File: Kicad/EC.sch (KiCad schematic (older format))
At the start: 23 parts, among them U1 MCP6244

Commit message: first pass at layout
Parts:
- removed POT1, POT2, POT3, POT4, POT5, POT6, TP7: CONN_1, symbol CONN_1
- removed R10: 10K, ~, symbol R
- added C8: .1u, ~, symbol C
- added D6: DIODE, ~, symbol DIODE
- added R12: 1K, ~, symbol R
- added R2: 1.5K 1%, ~, symbol R
- added R3, R4: 22K, ~, symbol R
- added unit 1 of U1
- renumbered C9 to C5, C10 to C6, C11 to C7, D3 to D7, D5 to D8
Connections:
- net AC_Shrunk: now also R3.2
- net EC_AIN: now also R12.1, U1.1, U1.2 (-); no longer C3.1, D7.2 (K), U1.13 (-)
- net EC_ProbeIN: now also R2.2
- net EC_Signal: now also R2.1
- net VGND: now also R3.1
- net pin 14 renamed R_Vout
- net pin 5 renamed W_Vin+
- net pin 6 renamed W_Vin-
- net W_Vin-: now also R4.2
- net pin 7 renamed W_Vout
- net W_Vout: now also R4.1
- new net DD: D6.1 (A), D7.2 (K), R12.2
- new net GND: C8.2, U1.11 (V-)
- new net RVin-: C3.1, D6.2 (K), U1.13 (-), U1.3 (+)
- new net Vclean: C8.1, U1.4 (V+)
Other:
- note added: "Probe"
- note added: "Step 1: Create an AC Signal"
- note added: "Step 2: Get EC Measurement"
- note added: "Step 3: Convert AC to DC"
- note removed: "Convert AC to DC"
- note removed: "Create an AC Signal"
- note removed: "Get EC Measurement"
- moved on the sheet: C3, D7, U1D

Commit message: 2nd iteration on layout
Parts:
- removed TP1, TP12, TP20: CONN_1, symbol CONN_1
- R2: value 1.5K 1% -> 1K 1%
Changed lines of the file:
@@
 Sheet 5 8
 Title ""
-Date "17 dec 2014"
+Date "18 dec 2014"
 Rev ""
 Comp ""
@@
 Step 3: Convert AC to DC
 $Comp
-L CONN_1 TP20
-U 1 1 54187FEE
-P 9000 2100
-F 0 "TP20" H 9080 2100 40  0000 L CNN
-F 1 "CONN_1" H 9000 2155 30  0001 C CNN
-F 2 "" H 9000 2100 60  0000 C CNN
-F 3 "" H 9000 2100 60  0000 C CNN
-	1    9000 2100
-	1    0    0    -1
-$EndComp
-Wire Wire Line
-	8850 2100 8850 2300
-Connection ~ 8850 2300
-Wire Wire Line
-	6050 1900 6050 2050
-Connection ~ 6050 2050
-$Comp
 L MCP6244 U1
 U 2 1 5419C202
@@
 Wire Wire Line
 	8750 4200 8850 4200
-$Comp
-L CONN_1 TP12
-U 1 1 544BE33F
-P 6050 1750
-F 0 "TP12" H 6130 1750 40  0000 L CNN
-F 1 "CONN_1" H 6050 1805 30  0001 C CNN
-F 2 "" H 6050 1750 60  0000 C CNN
-F 3 "" H 6050 1750 60  0000 C CNN
-	1    6050 1750
-	0    -1   -1   0
-$EndComp
 Text Label 8750 3050 0    60   ~ 0
 W_Vout
@@
 Connection ~ 6000 3100
 $Comp
-L CONN_1 TP1
-U 1 1 546E16C0
-P 4850 1800
-F 0 "TP1" H 4930 1800 40  0000 L CNN
-F 1 "CONN_1" H 4850 1855 30  0001 C CNN
-F 2 "" H 4850 1800 60  0000 C CNN
-F 3 "" H 4850 1800 60  0000 C CNN
-	1    4850 1800
-	1    0    0    -1
-$EndComp
-Wire Wire Line
-	4700 1800 4700 2150
-Connection ~ 4700 2150
-$Comp
 L R R4
 U 1 1 5486055C
@@
 P 5350 3100
 F 0 "R2" V 5430 3100 40  0000 C CNN
-F 1 "1.5K 1%" V 5357 3101 40  0000 C CNN
+F 1 "1K 1%" V 5357 3101 40  0000 C CNN
 F 2 "~" V 5280 3100 30  0000 C CNN
 F 3 "~" H 5350 3100 30  0000 C CNN

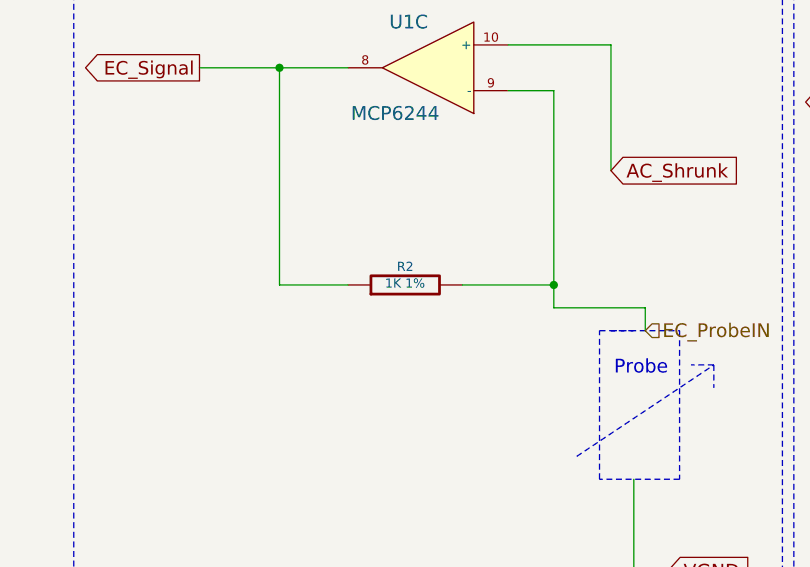
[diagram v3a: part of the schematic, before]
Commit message: changed diodes added test points
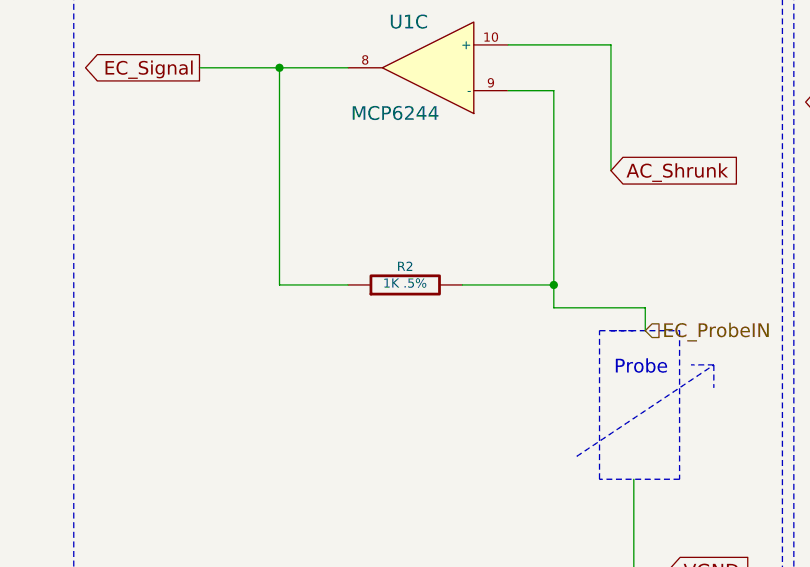
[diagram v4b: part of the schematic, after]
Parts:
- R2: value 1K 1% -> 1K .5%
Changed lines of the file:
@@
 Sheet 5 8
 Title ""
-Date "18 dec 2014"
+Date "20 dec 2014"
 Rev ""
 Comp ""
@@
 P 5350 3100
 F 0 "R2" V 5430 3100 40  0000 C CNN
-F 1 "1K 1%" V 5357 3101 40  0000 C CNN
+F 1 "1K .5%" V 5357 3101 40  0000 C CNN
 F 2 "~" V 5280 3100 30  0000 C CNN
 F 3 "~" H 5350 3100 30  0000 C CNN

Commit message: changes to layout after 12/22/2014 helpout
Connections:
- net AC_Shrunk: now also U1.3 (+); no longer U1.10 (+)
- net EC_AIN: now also U1.13 (-), U1.14; no longer U1.1, U1.2 (-)
- net EC_ProbeIN: now also U1.2 (-); no longer U1.9 (-)
- net EC_Signal: now also U1.1, U1.5 (+); no longer U1.12 (+), U1.8
- net GND: now also U1.11 (V-); no longer U1.11 (V-)
- net RVin-: now also U1.12 (+), U1.6 (-); no longer U1.13 (-), U1.3 (+)
- net R_Vout: now also U1.7; no longer U1.14
- net Vclean: now also U1.4 (V+); no longer U1.4 (V+)
- net W_Vin+: now also U1.10 (+); no longer U1.5 (+)
- net W_Vin-: now also U1.9 (-); no longer U1.6 (-)
- net W_Vout: now also U1.8; no longer U1.7
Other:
- moved on the sheet: C8
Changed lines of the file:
@@
 Sheet 5 8
 Title ""
-Date "20 dec 2014"
+Date "23 dec 2014"
 Rev ""
 Comp ""
@@
 $Comp
 L MCP6244 U1
-U 2 1 5419C202
+U 3 1 5419C202
 P 9500 2300
 F 0 "U1" H 9600 2500 60  0000 L CNN
@@
 F 2 "~" H 9600 2300 60  0000 C CNN
 F 3 "~" H 9600 2300 60  0000 C CNN
-	2    9500 2300
+	3    9500 2300
 	-1   0    0    -1
 $EndComp
 $Comp
 L MCP6244 U1
-U 3 1 5419C208
+U 1 1 5419C208
 P 5550 2150
 F 0 "U1" H 5650 2350 60  0000 L CNN
@@
 F 2 "~" H 5650 2150 60  0000 C CNN
 F 3 "~" H 5650 2150 60  0000 C CNN
-	3    5550 2150
+	1    5550 2150
 	-1   0    0    -1
 $EndComp
 $Comp
 L MCP6244 U1
-U 4 1 5419C20E
+U 2 1 5419C20E
 P 5750 5900
 F 0 "U1" H 5850 6100 60  0000 L CNN
@@
 F 2 "~" H 5850 5900 60  0000 C CNN
 F 3 "~" H 5850 5900 60  0000 C CNN
-	4    5750 5900
+	2    5750 5900
 	-1   0    0    -1
 $EndComp
@@
 L C C8
 U 1 1 548611AE
-P 2550 5450
-F 0 "C8" H 2550 5550 40  0000 L CNN
-F 1 ".1u" H 2556 5365 40  0000 L CNN
-F 2 "~" H 2588 5300 30  0000 C CNN
-F 3 "~" H 2550 5450 60  0000 C CNN
-	1    2550 5450
+P 5300 1600
+F 0 "C8" H 5300 1700 40  0000 L CNN
+F 1 ".1u" H 5306 1515 40  0000 L CNN
+F 2 "~" H 5338 1450 30  0000 C CNN
+F 3 "~" H 5300 1600 60  0000 C CNN
+	1    5300 1600
 	1    0    0    -1
 $EndComp
 Wire Wire Line
-	2800 5100 2800 5700
-Wire Wire Line
-	2550 5250 2800 5250
-Connection ~ 2800 5250
+	5550 1250 5550 1850
+Wire Wire Line
+	5300 1400 5550 1400
+Connection ~ 5550 1400
 Wire Notes Line
 	800  4600 7200 4600
@@
 Connection ~ 1650 6000
 Wire Wire Line
-	2550 5650 2550 5750
-Wire Wire Line
-	2800 6300 2800 6450
-Text GLabel 2800 5100 2    60   Input ~ 0
+	5300 1800 5300 1900
+Wire Wire Line
+	5550 2450 5550 2600
+Text GLabel 5550 1250 2    60   Input ~ 0
 Vclean
-Text GLabel 2800 6450 0    60   Input ~ 0
+Text GLabel 5550 2600 0    60   Input ~ 0
 GND
 Text GLabel 3400 6950 2    60   Input ~ 0
@@
 $Comp
 L MCP6244 U1
-U 1 1 549068E6
+U 4 1 549068E6
 P 2800 6000
 F 0 "U1" H 2900 6200 60  0000 L CNN
@@
 F 2 "~" H 2900 6000 60  0000 C CNN
 F 3 "~" H 2900 6000 60  0000 C CNN
-	1    2800 6000
-	-1   0    0    -1
-$EndComp
-Text GLabel 2550 5750 0    60   Input ~ 0
+	4    2800 6000
+	-1   0    0    -1
+$EndComp
+Text GLabel 5300 1900 0    60   Input ~ 0
 GND
 $EndSCHEMATC
